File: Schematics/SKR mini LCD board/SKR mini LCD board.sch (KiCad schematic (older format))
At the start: 9 parts, among them J1 Connector 5x2, SW1 Reset, U1 SSD1306 0.96\" OLED

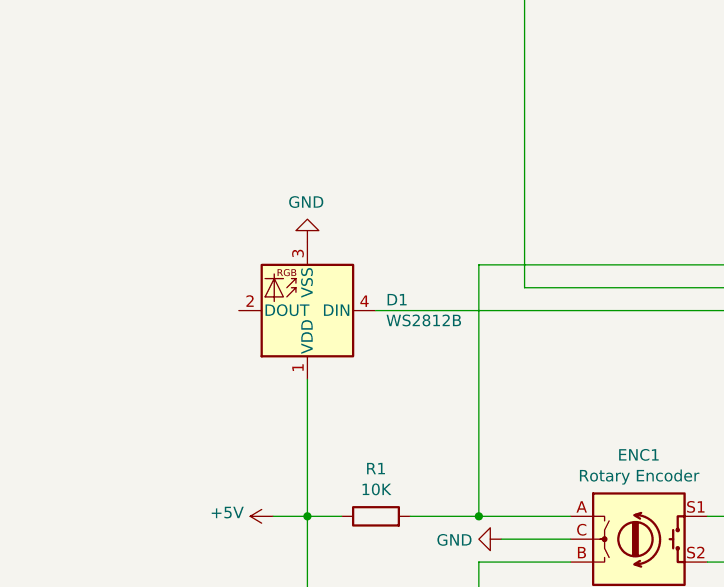
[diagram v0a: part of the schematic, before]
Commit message: Marked the WS2812 as optional
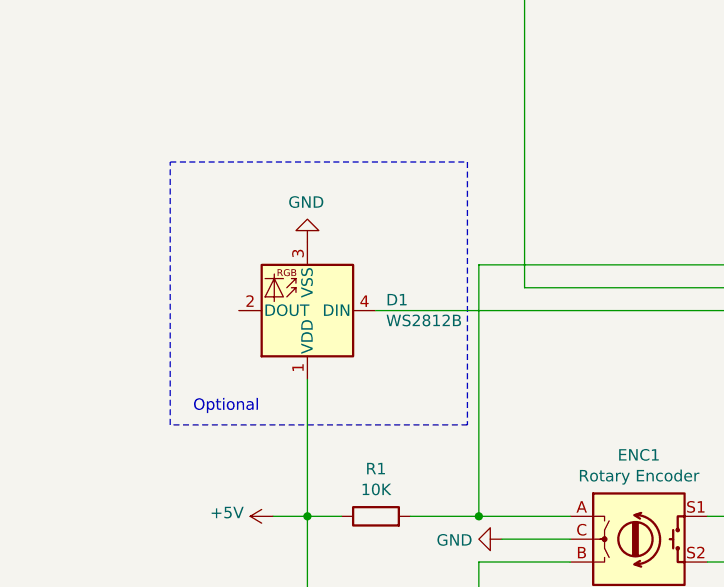
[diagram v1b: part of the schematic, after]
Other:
- note added: "Optional"
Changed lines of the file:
@@
 EESchema Schematic File Version 4
+LIBS:SKR mini LCD board-cache
 EELAYER 29 0
 EELAYER END
@@
 Wire Wire Line
 	3550 5400 3550 5950
+Wire Notes Line width 12
+	2950 3850 4250 3850
+Wire Notes Line width 12
+	4250 3850 4250 5000
+Wire Notes Line width 12
+	4250 5000 2950 5000
+Wire Notes Line width 12
+	2950 5000 2950 3850
+Text Notes 3050 4950 0    50   ~ 0
+Optional
 $EndSCHEMATC

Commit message: New version for preview. Added ESP32 custom board.
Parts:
- removed EXT2: Connector on Controller, symbol Connector_Generic:Conn_02x05_Odd_Even
- BZ1: footprint (none) -> Buzzer_Beeper:Buzzer_12x9.5RM7.6
- ENC1: footprint (none) -> Rotary_Encoder:RotaryEncoder_Alps_EC11E-Switch_Vertical_H20mm_CircularMountingHoles
- J1: footprint (none) -> Connector_PinSocket_2.54mm:PinSocket_2x05_P2.54mm_Vertical
- R1, R2: footprint (none) -> Resistor_THT:R_Axial_DIN0207_L6.3mm_D2.5mm_P10.16mm_Horizontal
- SW1: footprint (none) -> Button_Switch_THT:SW_PUSH_6mm_H7.3mm
- U1: footprint (none) -> Connector_PinHeader_2.54mm:PinHeader_1x04_P2.54mm_Vertical; symbol SSD1306_OLED-0.91-128x32:SSD1306 -> SKR-mini-LCD-board-rescue:SSD1306-SSD1306_OLED-0.91-128x32
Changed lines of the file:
@@
 $EndDescr
 $Comp
-L SSD1306_OLED-0.91-128x32:SSD1306 U1
+L SKR-mini-LCD-board-rescue:SSD1306-SSD1306_OLED-0.91-128x32 U1
 U 1 1 5D888A8E
 P 3150 3550
 F 0 "U1" V 1563 3867 60  0000 C CNN
 F 1 "SSD1306 0.96\" OLED" V 1669 3867 60  0000 C CNN
-F 2 "" H 3150 3550 60  0001 C CNN
+F 2 "Connector_PinHeader_2.54mm:PinHeader_1x04_P2.54mm_Vertical" H 3150 3550 60  0001 C CNN
 F 3 "" H 3150 3550 60  0001 C CNN
 	1    3150 3550
@@
 F 0 "ENC1" H 5000 5867 50  0000 C CNN
 F 1 "Rotary Encoder" H 5000 5776 50  0000 C CNN
-F 2 "" H 4850 5660 50  0001 C CNN
+F 2 "Rotary_Encoder:RotaryEncoder_Alps_EC11E-Switch_Vertical_H20mm_CircularMountingHoles" H 4850 5660 50  0001 C CNN
 F 3 "~" H 5000 5760 50  0001 C CNN
 	1    5000 5500
@@
 F 0 "J1" H 5900 4817 50  0000 C CNN
 F 1 "Connector 5x2" H 5900 4726 50  0000 C CNN
-F 2 "" H 5850 4400 50  0001 C CNN
+F 2 "Connector_PinSocket_2.54mm:PinSocket_2x05_P2.54mm_Vertical" H 5850 4400 50  0001 C CNN
 F 3 "~" H 5850 4400 50  0001 C CNN
 	1    5850 4400
@@
 F 0 "R1" V 4057 5400 50  0000 C CNN
 F 1 "10K" V 3966 5400 50  0000 C CNN
-F 2 "" V 3780 5400 50  0001 C CNN
+F 2 "Resistor_THT:R_Axial_DIN0207_L6.3mm_D2.5mm_P10.16mm_Horizontal" V 3780 5400 50  0001 C CNN
 F 3 "~" H 3850 5400 50  0001 C CNN
 	1    3850 5400
@@
 F 0 "BZ1" H 6200 4750 50  0000 L CNN
 F 1 "Buzzer" H 6200 4650 50  0000 L CNN
-F 2 "" V 6275 5050 50  0001 C CNN
+F 2 "Buzzer_Beeper:Buzzer_12x9.5RM7.6" V 6275 5050 50  0001 C CNN
 F 3 "~" V 6275 5050 50  0001 C CNN
 	1    6300 4950
@@
 F 0 "SW1" H 5050 1867 50  0000 C CNN
 F 1 "Reset" H 5050 1776 50  0000 C CNN
-F 2 "" H 5050 1600 50  0001 C CNN
+F 2 "Button_Switch_THT:SW_PUSH_6mm_H7.3mm" H 5050 1600 50  0001 C CNN
 F 3 "~" H 5050 1600 50  0001 C CNN
 	1    5050 1600
@@
 $EndComp
 $Comp
-L power:+5V #PWR?
+L power:+5V #PWR0101
 U 1 1 5D89576B
 P 3400 5400
-F 0 "#PWR?" H 3400 5250 50  0001 C CNN
+F 0 "#PWR0101" H 3400 5250 50  0001 C CNN
 F 1 "+5V" V 3415 5528 50  0000 L CNN
 F 2 "" H 3400 5400 50  0001 C CNN
@@
 $EndComp
 $Comp
-L power:+5V #PWR?
+L power:+5V #PWR0102
 U 1 1 5D896CC4
 P 5450 3800
-F 0 "#PWR?" H 5450 3650 50  0001 C CNN
+F 0 "#PWR0102" H 5450 3650 50  0001 C CNN
 F 1 "+5V" H 5465 3973 50  0000 C CNN
 F 2 "" H 5450 3800 50  0001 C CNN
@@
 $EndComp
 $Comp
-L power:+5V #PWR?
+L power:+5V #PWR0103
 U 1 1 5D89755D
 P 3500 2100
-F 0 "#PWR?" H 3500 1950 50  0001 C CNN
+F 0 "#PWR0103" H 3500 1950 50  0001 C CNN
 F 1 "+5V" H 3515 2273 50  0000 C CNN
 F 2 "" H 3500 2100 50  0001 C CNN
@@
 $EndComp
 $Comp
-L power:GND #PWR?
+L power:GND #PWR0104
 U 1 1 5D897F1D
 P 4600 1850
-F 0 "#PWR?" H 4600 1600 50  0001 C CNN
+F 0 "#PWR0104" H 4600 1600 50  0001 C CNN
 F 1 "GND" H 4605 1677 50  0000 C CNN
 F 2 "" H 4600 1850 50  0001 C CNN
@@
 $EndComp
 $Comp
-L power:GND #PWR?
+L power:GND #PWR0105
 U 1 1 5D898A40
 P 3550 2500
-F 0 "#PWR?" H 3550 2250 50  0001 C CNN
+F 0 "#PWR0105" H 3550 2250 50  0001 C CNN
 F 1 "GND" H 3555 2327 50  0000 C CNN
 F 2 "" H 3550 2500 50  0001 C CNN
@@
 $EndComp
 $Comp
-L power:GND #PWR?
+L power:GND #PWR0106
 U 1 1 5D899BAF
 P 5650 5700
-F 0 "#PWR?" H 5650 5450 50  0001 C CNN
+F 0 "#PWR0106" H 5650 5450 50  0001 C CNN
 F 1 "GND" H 5655 5527 50  0000 C CNN
 F 2 "" H 5650 5700 50  0001 C CNN
@@
 $EndComp
 $Comp
-L power:GND #PWR?
+L power:GND #PWR0107
 U 1 1 5D89A417
 P 5950 5150
-F 0 "#PWR?" H 5950 4900 50  0001 C CNN
+F 0 "#PWR0107" H 5950 4900 50  0001 C CNN
 F 1 "GND" H 5955 4977 50  0000 C CNN
 F 2 "" H 5950 5150 50  0001 C CNN
@@
 	5950 5050 5950 5150
 $Comp
-L power:GND #PWR?
+L power:GND #PWR0108
 U 1 1 5D89B98C
 P 6250 3800
-F 0 "#PWR?" H 6250 3550 50  0001 C CNN
+F 0 "#PWR0108" H 6250 3550 50  0001 C CNN
 F 1 "GND" H 6255 3627 50  0000 C CNN
 F 2 "" H 6250 3800 50  0001 C CNN
@@
 F 0 "R2" V 4057 5950 50  0000 C CNN
 F 1 "10K" V 3966 5950 50  0000 C CNN
-F 2 "" V 3780 5950 50  0001 C CNN
+F 2 "Resistor_THT:R_Axial_DIN0207_L6.3mm_D2.5mm_P10.16mm_Horizontal" V 3780 5950 50  0001 C CNN
 F 3 "~" H 3850 5950 50  0001 C CNN
 	1    3850 5950
@@
 	6150 4600 6150 4850
 $Comp
-L power:GND #PWR?
+L power:GND #PWR0109
 U 1 1 5D8A9A64
 P 4400 5500
-F 0 "#PWR?" H 4400 5250 50  0001 C CNN
+F 0 "#PWR0109" H 4400 5250 50  0001 C CNN
 F 1 "GND" V 4405 5372 50  0000 R CNN
 F 2 "" H 4400 5500 50  0001 C CNN
@@
 $EndComp
 $Comp
-L Connector_Generic:Conn_02x05_Odd_Even EXT2
+L Connector_Generic:Conn_02x05_Odd_Even #EXT2
 U 1 1 5D8AB540
 P 6250 1700
-F 0 "EXT2" H 6300 2117 50  0000 C CNN
+F 0 "#EXT2" H 6300 2117 50  0000 C CNN
 F 1 "Connector on Controller" H 6300 2026 50  0000 C CNN
 F 2 "" H 6250 1700 50  0001 C CNN
@@
 	3850 4500 5650 4500
 $Comp
-L power:GND #PWR?
+L power:GND #PWR0110
 U 1 1 5D8C682F
 P 3550 4200
-F 0 "#PWR?" H 3550 3950 50  0001 C CNN
+F 0 "#PWR0110" H 3550 3950 50  0001 C CNN
 F 1 "GND" H 3555 4027 50  0000 C CNN
 F 2 "" H 3550 4200 50  0001 C CNN
